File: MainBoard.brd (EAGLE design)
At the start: 100 x 100 mm, 66 parts, among them IC4 DS1307, IC7 74HC595D, IC8 74HC595D, IC9 74HC595D, U2 ATMEGA328P-AU

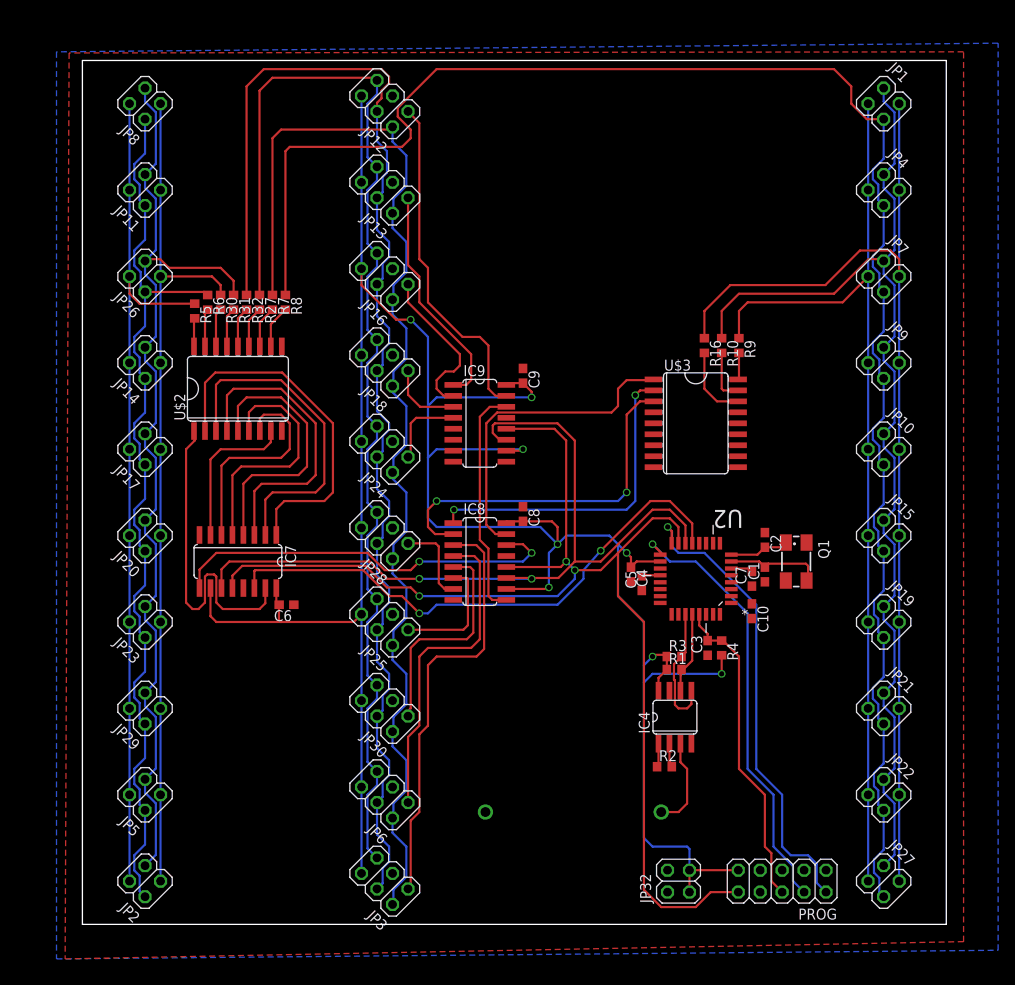
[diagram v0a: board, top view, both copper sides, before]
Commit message: - Added 3 Buttons - Organized Schematic
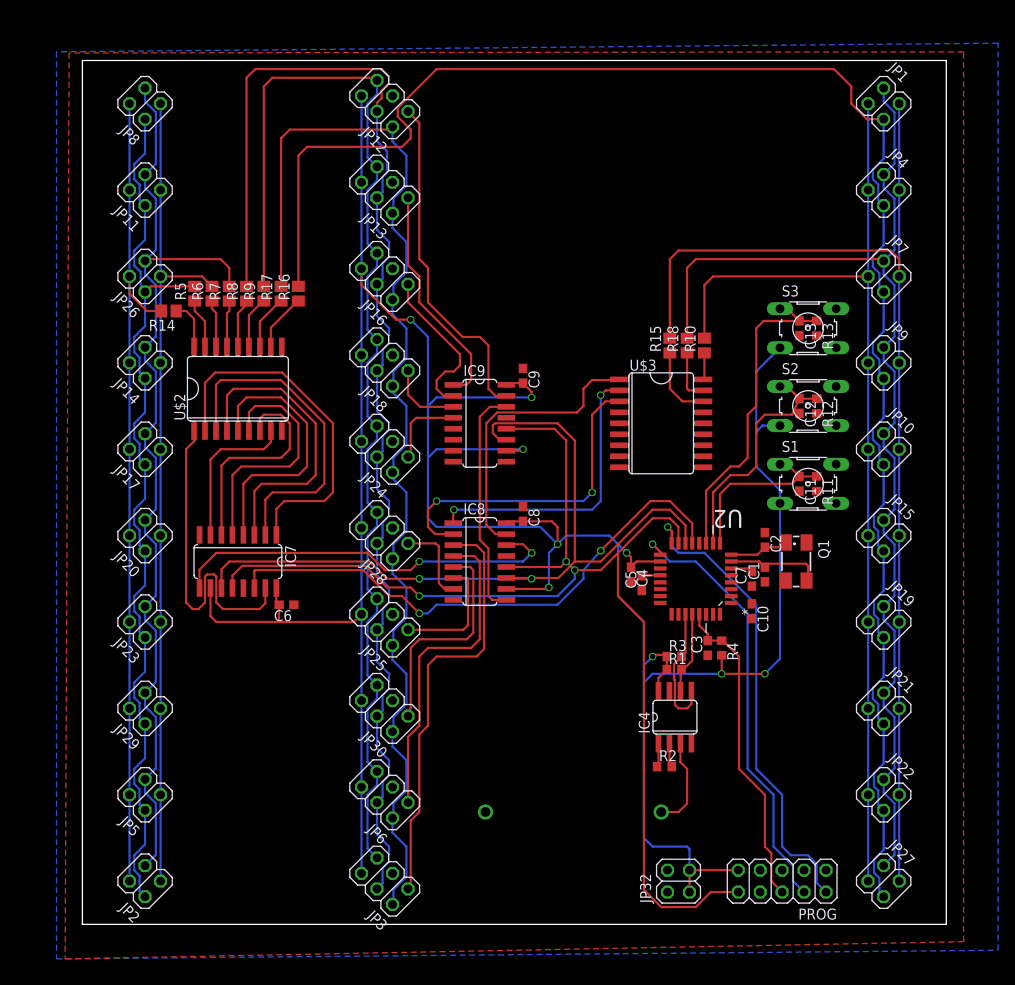
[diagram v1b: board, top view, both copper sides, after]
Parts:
- removed R27, R30, R31, R32: 47, rcl:R0603
- added C11, C12, C13: 100nF, eagle-ltspice:C0603
- added R11, R12, R13: 10k, eagle-ltspice:R0603
- added R14, R15, R17, R18: 5R6, resistor:R0805
- added S1, S2, S3: (no value), switch-omron:B3F-10XX
- C3: value 47uF -> 100uF
- R10, R16, R5, R6, R7, R8, R9: value 47 -> 5R6; device rcl:R0603 -> resistor:R0805
- R2: value (none) -> r2
- moved R9 55.3 mm to (21.0, 73.0), turned to 90 degrees
- moved R16 47.4 mm to (25.0, 73.0), turned to 90 degrees
- moved R7 5.10 mm to (17.0, 73.0), turned to 90 degrees
- moved R8 4.61 mm to (19.0, 73.0), turned to 90 degrees
- moved U$3 4.00 mm to (67.0, 58.0)
- moved R10 2.00 mm to (72.0, 67.0), turned to 90 degrees
- moved R5 2.00 mm to (13.0, 73.0), turned to 90 degrees
- moved R6 1.12 mm to (15.0, 73.0), turned to 90 degrees
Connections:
- new net N$14: C12.1, R12.1, S2.1, U2.10
- new net N$15: C13.1, R13.1, S3.1, U2.11
- new net N$7: C11.1, R11.1, S1.1, U2.9
- net GND: now also C11.2, C12.2, C13.2, R11.2, R12.2, R13.2
- net N$1: now also R6.1; no longer R30.2
- net N$11: now also R14.1; no longer R5.2
- net N$2: now also R17.1; no longer R7.2
- net N$22: now also R10.1; no longer R9.2
- net N$23: now also R18.1; no longer R10.2
- net N$24: now also R15.1; no longer R16.2
- net N$3: now also R17.2; no longer R7.1
- net N$47: now also R6.2; no longer R30.1
- net N$50: now also R7.1; no longer R31.2
- net N$51: now also R7.2; no longer R31.1
- net N$52: now also R9.2; no longer R27.1
- net N$53: now also R16.1; no longer R8.2
- net N$54: now also R5.1; no longer R6.2
- net N$6: now also R9.1; no longer R27.2
- net N$71: now also R10.2; no longer R9.1
- net N$72: now also R8.2; no longer R32.1
- net N$74: now also R16.2; no longer R8.1
- net N$76: now also R18.2; no longer R10.1
- net N$77: now also R15.2; no longer R16.1
- net N$8: now also R8.1; no longer R32.2
- net N$80: now also R5.2; no longer R6.1
- net N$81: now also R14.2; no longer R5.1
- net VCC: now also S1.3, S2.3, S3.3
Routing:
- net VCC: track 300.5 -> 350.8 mm, vias 8 -> 9
- net N$15: track 0.00 -> 38.1 mm
- net N$14: track 0.00 -> 28.6 mm
- net N$7: track 0.00 -> 20.6 mm
- net N$77: track 121.0 -> 128.5 mm
- net N$76: track 123.8 -> 130.7 mm
- net N$71: track 109.8 -> 115.5 mm
- net N$45: track 37.1 -> 33.1 mm
- net N$49: track 41.8 -> 37.8 mm
- net N$48: track 37.6 -> 33.6 mm
- net N$81: track 100.0 -> 96.5 mm
- net N$74: track 196.5 -> 193.7 mm
- net N$11: track 3.28 -> 5.63 mm
- net N$47: track 98.5 -> 96.4 mm
- net N$3: track 134.5 -> 132.5 mm
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
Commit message: Finished Routing an Panelizing
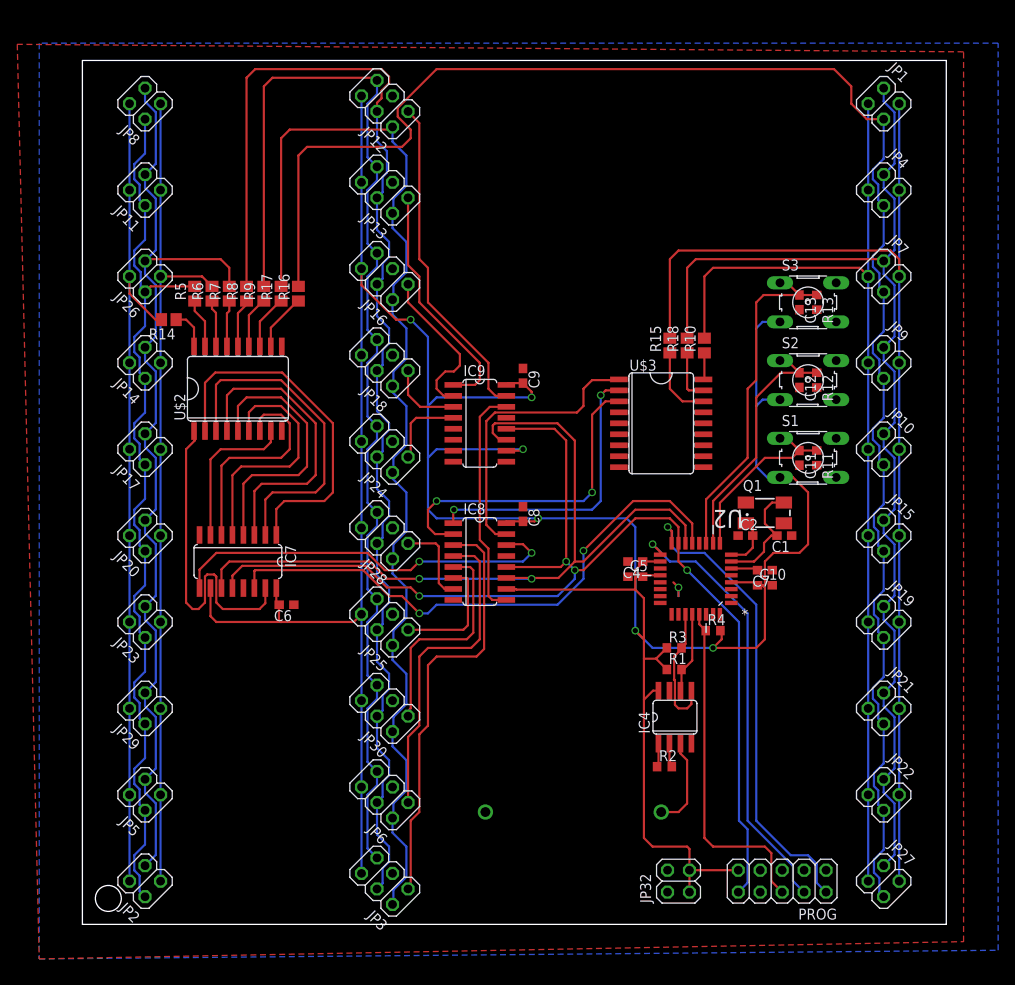
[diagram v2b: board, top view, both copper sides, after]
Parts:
- removed C3: 100uF, eagle-ltspice:C0603
- moved Q1 6.69 mm to (79.0, 47.6), turned to 0 degrees
- moved C1 5.03 mm to (81.2, 45.0), turned to 180 degrees
- moved C10 3.35 mm to (79.0, 39.2), turned to 0 degrees
- moved C11 3.00 mm to (83.0, 54.0)
- moved C12 3.00 mm to (83.0, 63.0)
- moved C13 3.00 mm to (83.0, 72.0)
- moved R11 3.00 mm to (85.0, 54.0)
- moved R12 3.00 mm to (85.0, 63.0)
- moved R13 3.00 mm to (85.0, 72.0)
- moved S1 3.00 mm to (84.0, 54.0)
- moved S2 3.00 mm to (84.0, 63.0)
- moved S3 3.00 mm to (84.0, 72.0)
- moved C2 2.30 mm to (76.8, 45.0), turned to 0 degrees
- moved R4 2.24 mm to (73.0, 34.0), turned to 0 degrees
- moved C7 1.80 mm to (79.0, 41.0), turned to 180 degrees
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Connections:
- removed net +5V: C10.1, C7.2, U2.4, U2.6
- removed net N$4: C5.2, U2.20
- net GND: no longer C3.1
- net N$5: no longer C3.2
- net VCC: now also C10.1, C5.2, C7.2, U2.20, U2.4, U2.6
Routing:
- net VCC: track 350.8 -> 374.4 mm, vias 9 -> 6
- net RCK: track 144.4 -> 135.8 mm, vias 3 -> 4
- net GND: track 0.29 -> 3.13 mm, vias 0 -> 1
- net N$5: track 37.2 -> 39.8 mm
- net +5V: track 2.53 -> 0.00 mm
- net N$15: track 38.1 -> 40.5 mm
- net N$4: track 2.16 -> 0.00 mm
- net N$44: track 11.1 -> 13.2 mm
- net N$46: track 7.61 -> 5.98 mm
- net N$71: track 115.5 -> 117.0 mm
- net N$40: track 26.4 -> 27.8 mm
- net N$14: track 28.6 -> 30.0 mm
- net DATA: track 64.2 -> 65.4 mm
- net N$38: track 39.5 -> 38.4 mm
- net N$11: track 5.63 -> 4.63 mm
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
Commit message: Changed tolerances on ledboard and mainboard
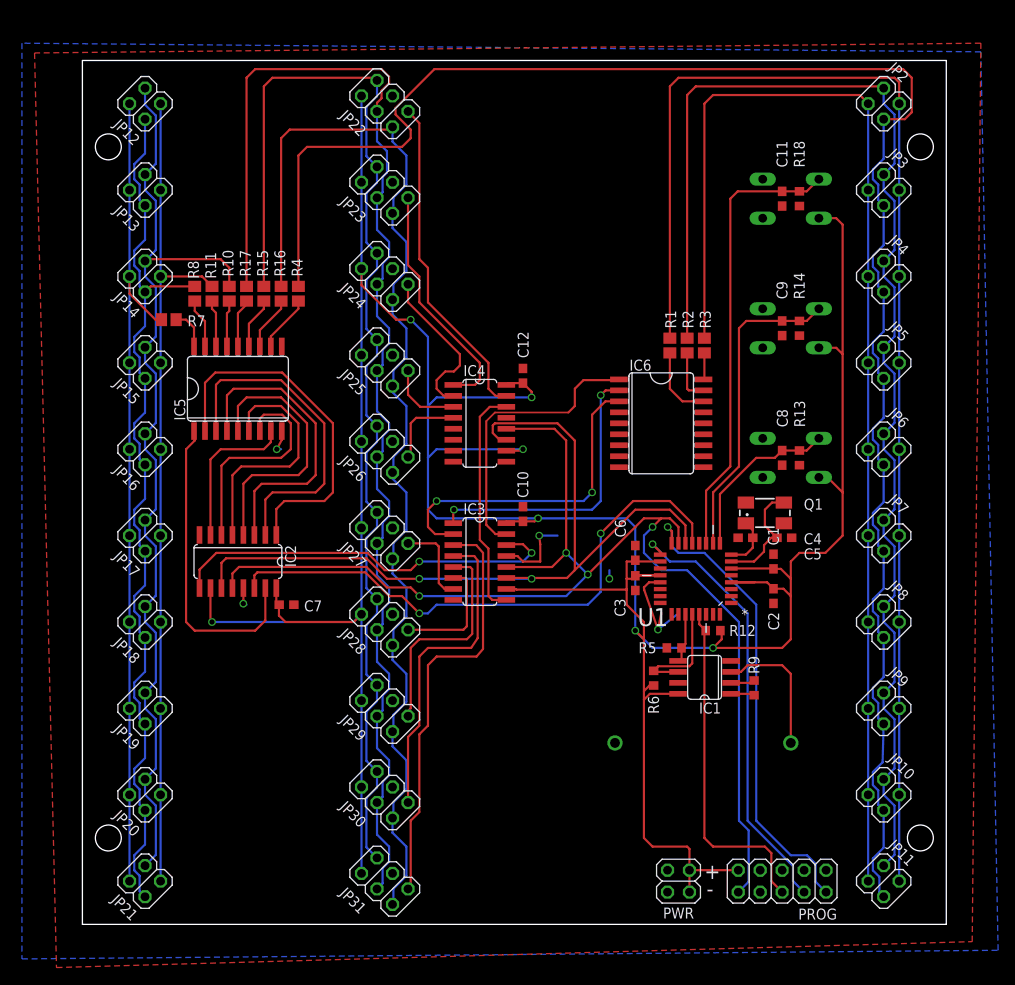
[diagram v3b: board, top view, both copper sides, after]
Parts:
- removed C13: 100nF, eagle-ltspice:C0603
- removed IC9: 74HC595D, 74xx-eu:SO16
- removed JP1: (no value), pinhead:2X02
- removed U$4: CR2032, 2032:CR2023
- added C3: 100uF, eagle-ltspice:C0603
- added IC1: DS1307, dallas:SOIC-8
- added JP31: (no value), pinhead:2X03
- added U$1: CR2032, 2032:CR2023
- C1, C2: value 22uF -> 100uF
- C12: value 100nF -> 100uF
- C4, C5: value 100uF -> 22uF
- C8, C9: value 100uF -> 100nF
- IC4: value DS1307 -> 74HC595D; device dallas:SOIC-8 -> 74xx-eu:SO16
- JP12, JP13, JP16, JP18, JP3, JP6: device pinhead:2X03 -> pinhead:2X02
- JP22, JP23, JP26, JP27, JP29: device pinhead:2X02 -> pinhead:2X03
- R1, R11, R3, R4: value 10k -> 5R6; device eagle-ltspice:R0603 -> resistor:R0805
- R14, R18, R5, R6: value 5R6 -> 10k; device resistor:R0805 -> eagle-ltspice:R0603
- R2: value r2 -> 5R6; device eagle-ltspice:R0603 -> resistor:R0805
- R9: value 5R6 -> r2; device resistor:R0805 -> eagle-ltspice:R0603
- moved JP2 124.1 mm to (92.8, 95.0), turned to 315 degrees
- moved JP11 117.1 mm to (92.8, 5.00), turned to 315 degrees
- moved JP8 104.5 mm to (92.8, 35.0), turned to 315 degrees
- moved JP5 99.0 mm to (92.8, 65.0), turned to 315 degrees
- moved JP22 98.7 mm to (35.0, 95.0), turned to 135 degrees
- moved JP3 98.7 mm to (92.8, 85.0), turned to 315 degrees
- moved JP15 87.8 mm to (7.25, 65.0), turned to 135 degrees
- moved JP21 87.8 mm to (7.25, 5.00), turned to 135 degrees
- moved JP19 86.1 mm to (7.25, 25.0), turned to 135 degrees
- moved R14 73.0 mm to (83.0, 69.0), turned to 270 degrees
- moved R9 72.8 mm to (77.8, 27.4)
- moved R11 72.5 mm to (15.0, 73.0), turned to 90 degrees
- moved JP27 70.2 mm to (35.0, 45.0), turned to 135 degrees
- moved JP6 70.2 mm to (92.8, 55.0), turned to 315 degrees
- moved R5 69.0 mm to (68.5, 32.0), turned to 0 degrees
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- renumbered IC7 to IC2, IC8 to IC3, JP32 to PWR, U$2 to IC5, U$3 to IC6, U2 to U1
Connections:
- net GND: now also C10.1, C12.1, C2.2, C3.1, C4.1, C6.2, C8.2, C9.2, IC1.4, IC4.13, IC4.8, JP22.3, JP23.3, JP26.3, JP27.3, JP29.3, JP31.3, R14.2, R18.2, U$1.GND@1; no longer C10.2, C12.2, C13.2, C2.1, C4.2, C6.1, C8.1, C9.1, IC4.4, IC9.13, IC9.8, JP12.3, JP13.3, JP16.3, JP18.3, JP3.3, JP6.3, R11.2, R12.2, U$4.GND@1
- net N$1: now also R11.1; no longer R6.1
- net N$11: now also R7.1; no longer R14.1
- net N$14: now also C9.1, R14.1; no longer C12.1, R12.1
- net N$15: now also C11.1, R18.1; no longer C13.1, R13.1
- net N$2: now also R16.1; no longer R17.1
- net N$22: now also R3.1; no longer R10.1
- net N$23: now also R2.1; no longer R18.1
- net N$24: now also R1.1; no longer R15.1
- net N$26: now also JP31.1; no longer JP3.1
- net N$27: now also IC1.3, U$1.P$2; no longer IC4.3, U$4.P$2
- net N$3: now also JP22.2, JP23.2, JP26.2, JP27.2, JP29.2, JP31.2, R16.2; no longer JP12.2, JP13.2, JP16.2, JP18.2, JP3.2, JP6.2, R17.2
- net N$32: now also IC1.5, R5.2; no longer IC4.5, R3.2
- net N$33: now also IC1.2, R9.2; no longer IC4.2, R2.2
- net N$37: now also IC1.1, R9.1; no longer IC4.1, R2.1
- net N$38: now also IC4.15, JP22.1; no longer IC9.15, JP12.1
- net N$39: now also IC1.6, R6.2; no longer IC4.6, R1.2
- net N$40: now also IC4.1, JP23.1; no longer IC9.1, JP13.1
- net N$44: now also C4.2; no longer C1.2
- net N$46: now also C5.2; no longer C2.2
- net N$47: now also JP12.1, JP13.1, JP15.1, JP16.1, JP18.1, JP19.1, JP21.1, R11.2; no longer JP11.1, JP2.1, JP23.1, JP26.1, JP29.1, JP5.1, JP8.1, R6.2
- net N$5: now also R12.1; no longer R4.1
- net N$50: now also R10.1; no longer R7.1
- net N$51: now also JP12.3, JP13.3, JP15.3, JP16.3, JP18.3, JP19.3, JP21.3, R10.2; no longer JP11.3, JP2.3, JP23.3, JP26.3, JP29.3, JP5.3, JP8.3, R7.2
- net N$52: now also JP22.5, JP23.5, JP26.5, JP27.5, JP29.5, JP31.5, R15.2; no longer JP12.5, JP13.5, JP16.5, JP18.5, JP3.5, JP6.5, R9.2
- net N$53: now also R4.1; no longer R16.1
- net N$54: now also R8.1; no longer R5.1
- net N$56: now also IC4.2, JP24.1; no longer IC9.2, JP16.1
- net N$57: now also IC4.3, JP25.1; no longer IC9.3, JP18.1
- net N$58: now also IC4.4, JP26.1; no longer IC9.4, JP24.1
- net N$6: now also R15.1; no longer R9.1
- net N$60: now also JP27.1; no longer JP28.1
- net N$62: now also JP28.1; no longer JP25.1
- net N$69: now also JP29.1; no longer JP30.1
- net N$7: now also C8.1, R13.1; no longer C11.1, R11.1
- net N$70: now also JP30.1; no longer JP6.1
- net N$71: now also JP11.1, JP2.1, JP3.1, JP5.1, JP6.1, JP8.1, R3.2; no longer JP1.1, JP15.1, JP19.1, JP21.1, JP22.1, JP27.1, R10.2
- net N$72: now also JP22.4, JP23.4, JP26.4, JP27.4, JP29.4, JP31.4, R17.2; no longer JP12.4, JP13.4, JP16.4, JP18.4, JP3.4, JP6.4, R8.2
- net N$74: now also JP11.3, JP2.3, JP3.3, JP5.3, JP6.3, JP8.3, R4.2; no longer JP1.3, JP15.3, JP19.3, JP21.3, JP22.3, JP27.3, R16.2
- net N$76: now also JP11.2, JP2.2, JP3.2, JP5.2, JP6.2, JP8.2, R2.2; no longer JP1.2, JP15.2, JP19.2, JP21.2, JP22.2, JP27.2, R18.2
- net N$77: now also JP11.4, JP2.4, JP3.4, JP5.4, JP6.4, JP8.4, R1.2; no longer JP1.4, JP15.4, JP19.4, JP21.4, JP22.4, JP27.4, R15.2
- net N$8: now also R17.1; no longer R8.1
- net N$80: now also JP12.2, JP13.2, JP15.2, JP16.2, JP18.2, JP19.2, JP21.2, R8.2; no longer JP11.2, JP2.2, JP23.2, JP26.2, JP29.2, JP5.2, JP8.2, R5.2
- net N$81: now also JP12.4, JP13.4, JP15.4, JP16.4, JP18.4, JP19.4, JP21.4, R7.2; no longer JP11.4, JP2.4, JP23.4, JP26.4, JP29.4, JP5.4, JP8.4, R14.2
- net N$9: now also IC4.14; no longer IC9.14
- net RCK: now also IC4.12; no longer IC9.12
- net SCK: now also IC4.11; no longer IC9.11
- net VCC: now also C1.2, C10.2, C12.2, C2.1, C3.2, C6.1, IC1.8, IC4.10, IC4.16, JP22.6, JP23.6, JP26.6, JP27.6, JP29.6, JP31.6, R12.2, R5.1, R6.1; no longer C10.1, C4.1, C5.2, C6.2, C8.2, C9.2, IC4.8, IC9.10, IC9.16, JP12.6, JP13.6, JP16.6, JP18.6, JP3.6, JP6.6, R1.1, R3.1, R4.2
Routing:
- net VCC: track 374.4 -> 411.0 mm, vias 6 -> 7
- net GND: track 3.13 -> 28.2 mm, vias 1 -> 5
- net N$77: track 128.5 -> 148.8 mm
- net N$76: track 130.7 -> 150.7 mm
- net N$71: track 117.0 -> 136.9 mm
- net N$15: track 40.5 -> 52.2 mm
- net N$32: track 15.5 -> 6.19 mm
- net N$74: track 193.7 -> 202.1 mm
- net RCK: track 135.8 -> 144.1 mm
- net N$14: track 30.0 -> 36.3 mm
- net N$27: track 10.6 -> 15.6 mm
- net N$39: track 9.52 -> 13.5 mm
- net N$13: track 38.8 -> 36.5 mm
- net SCK: track 93.4 -> 95.2 mm
- net DATA: track 65.4 -> 67.0 mm
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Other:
- board text added: "+"
- board text added: "-"

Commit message: Finalizing prototype
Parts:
- removed R9: r2, eagle-ltspice:R0603
- added U$2: CC5V-T1A, cc5v-t1a:CC5V-T1A
- moved R6 6.84 mm to (72.0, 32.0), turned to 180 degrees
- moved C8 6.00 mm to (81.0, 60.0)
- moved C9 6.00 mm to (81.0, 75.0)
- moved IC6 6.00 mm to (67.0, 64.0)
- moved R1 6.00 mm to (68.0, 73.0)
- moved R13 6.00 mm to (83.0, 60.0)
- moved R14 6.00 mm to (83.0, 75.0)
- moved R2 6.00 mm to (70.0, 73.0)
- moved R3 6.00 mm to (72.0, 73.0)
- moved S1 6.00 mm to (82.0, 60.0)
- moved S2 6.00 mm to (82.0, 75.0)
- moved R7 4.24 mm to (13.0, 73.0), turned to 90 degrees
- moved C2 2.50 mm to (77.5, 38.0)
- moved R10 2.00 mm to (19.0, 73.0)
- moved R11 2.00 mm to (17.0, 73.0)
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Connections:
- removed net N$33: IC1.2, R9.2
- removed net N$37: IC1.1, R9.1
- new net N$16: IC1.1, U$2.P$1
- new net N$4: IC1.2, U$2.P$2
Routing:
- net N$51: track 111.7 -> 136.5 mm
- net N$47: track 96.4 -> 118.5 mm
- net N$81: track 96.9 -> 117.5 mm
- net N$80: track 105.3 -> 125.7 mm
- net GND: track 28.2 -> 16.8 mm
- net N$7: track 19.8 -> 26.0 mm
- net N$77: track 148.8 -> 142.8 mm
- net N$76: track 150.7 -> 144.7 mm
- net N$71: track 136.9 -> 130.9 mm
- net N$14: track 36.3 -> 42.3 mm
- net N$48: track 33.6 -> 39.6 mm
- net N$49: track 37.8 -> 43.7 mm
- net N$45: track 33.3 -> 38.8 mm, vias 0 -> 2
- net SCK: track 95.2 -> 90.2 mm, vias 2 -> 3
- net N$16: track 0.00 -> 4.57 mm
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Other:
- board text added: "Bottom"
- board text added: "MainBoard v1.0"

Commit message: Final layout of prototype
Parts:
- removed Q1: (no value), crystal:CTS406
- added U$3: 16,00-MT, 1600MT:16,00-MT
- C4, C5: value 22uF -> (none); device eagle-ltspice:C0603 -> rcl:C0603
- moved C11 6.00 mm to (81.0, 90.0)
- moved R18 6.00 mm to (83.0, 90.0)
- moved S3 6.00 mm to (82.0, 90.0)
- moved C4 1.95 mm to (78.4, 42.5)
- moved C5 1.25 mm to (75.8, 45.0), turned to 270 degrees
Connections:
- removed net N$46: C5.2, Q1.1, U1.8
- new net N$17: C5.2, U$3.P2, U1.8
- net N$44: now also U$3.P1; no longer Q1.3
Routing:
- net VCC: track 406.6 -> 412.6 mm
- net N$15: track 52.2 -> 58.2 mm
- net N$44: track 11.0 -> 6.99 mm
- net N$17: track 0.00 -> 3.29 mm
- net N$46: track 3.29 -> 0.00 mm
